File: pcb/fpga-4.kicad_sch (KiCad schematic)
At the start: 15 parts, among them U7 XC7A100T-FGG484

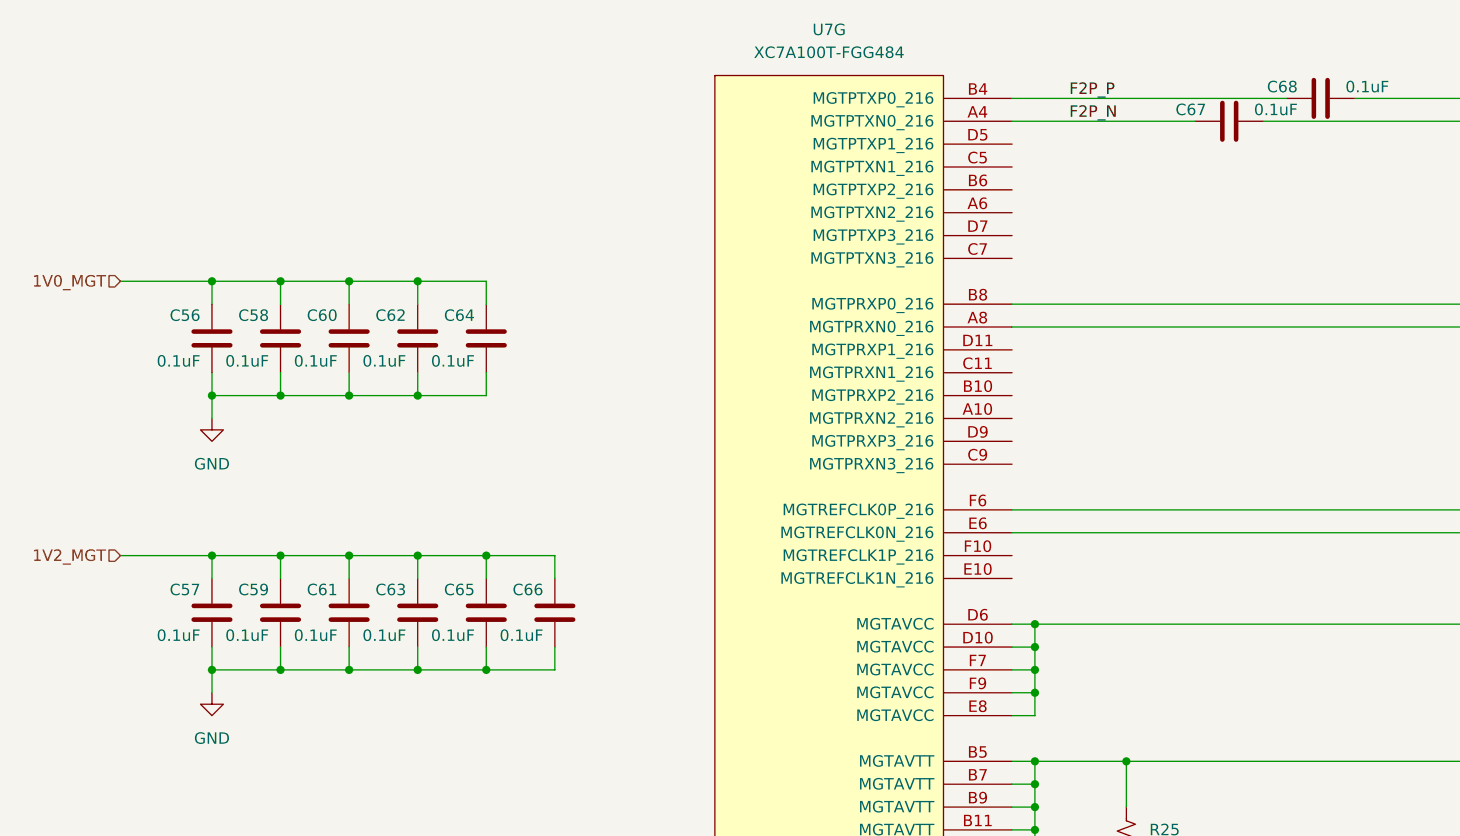
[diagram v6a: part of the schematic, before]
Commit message: added mig ddr pinout constraints
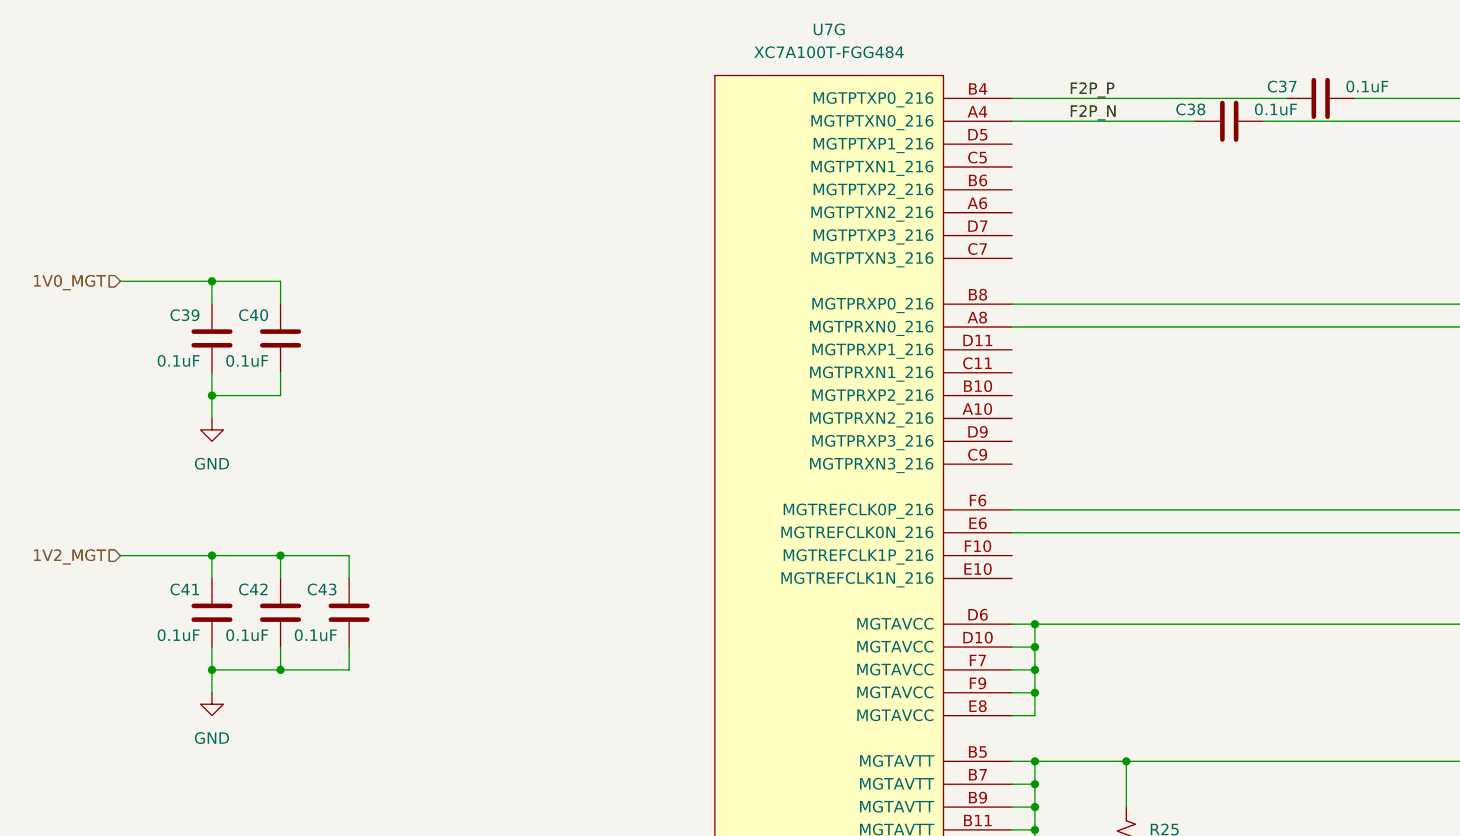
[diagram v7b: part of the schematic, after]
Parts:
- removed C60, C62, C63, C64, C65, C66: 0.1uF, Capacitor_SMD:C_0402_1005Metric, symbol library:C
- renumbered C68 to C37, C67 to C38, C56 to C39, C58 to C40, C57 to C41, C59 to C42, C61 to C43

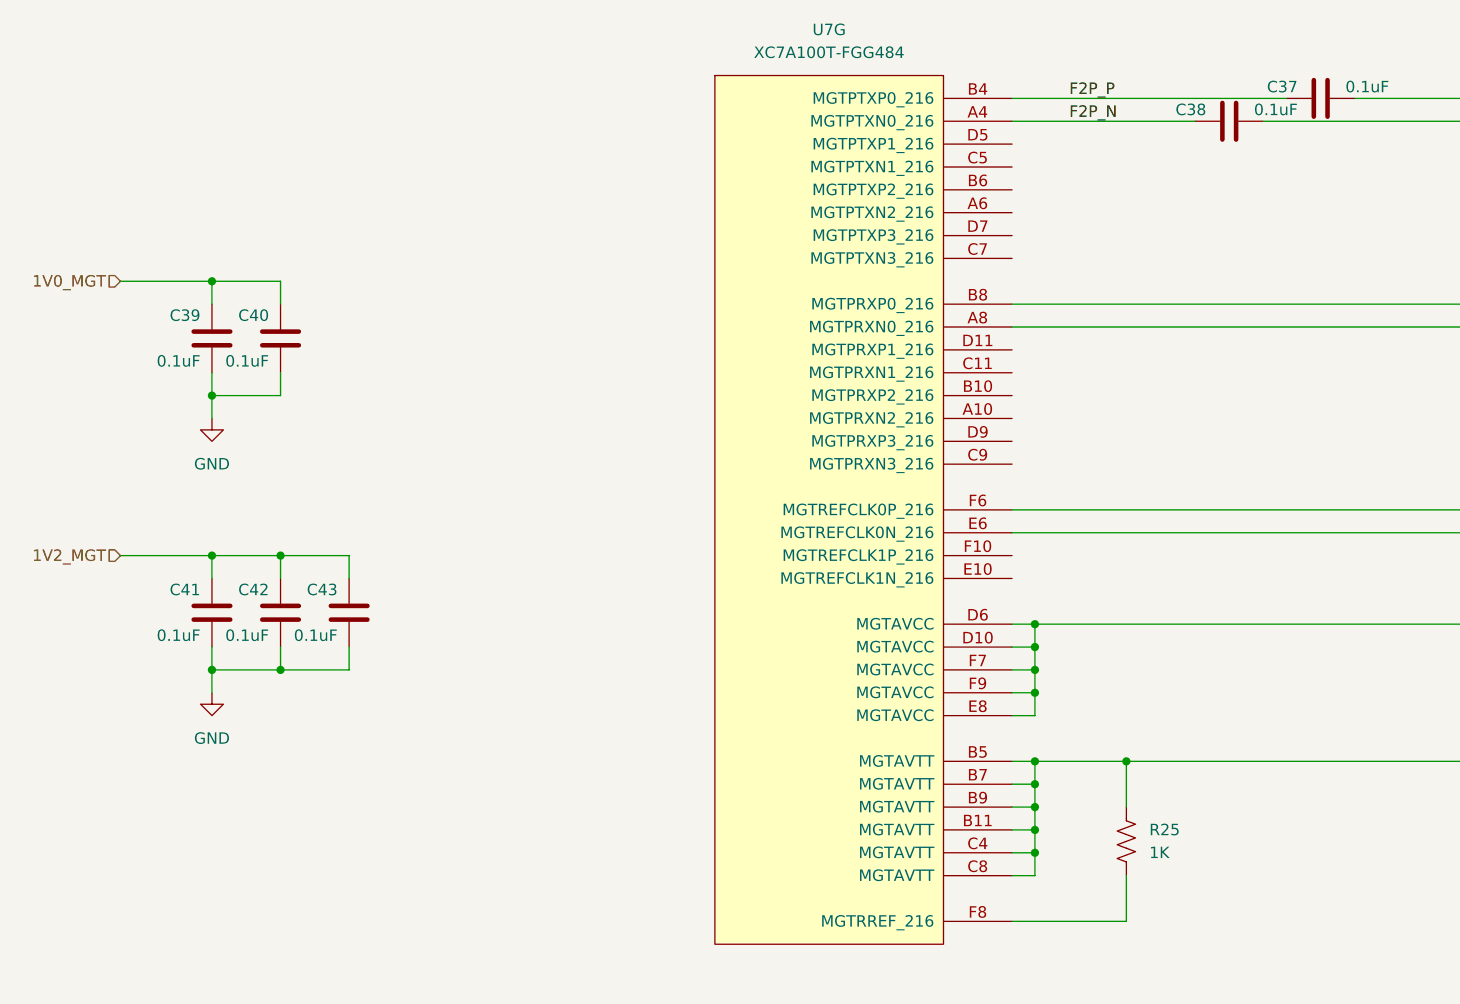
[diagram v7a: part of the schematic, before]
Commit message: restructured power, power plane layout
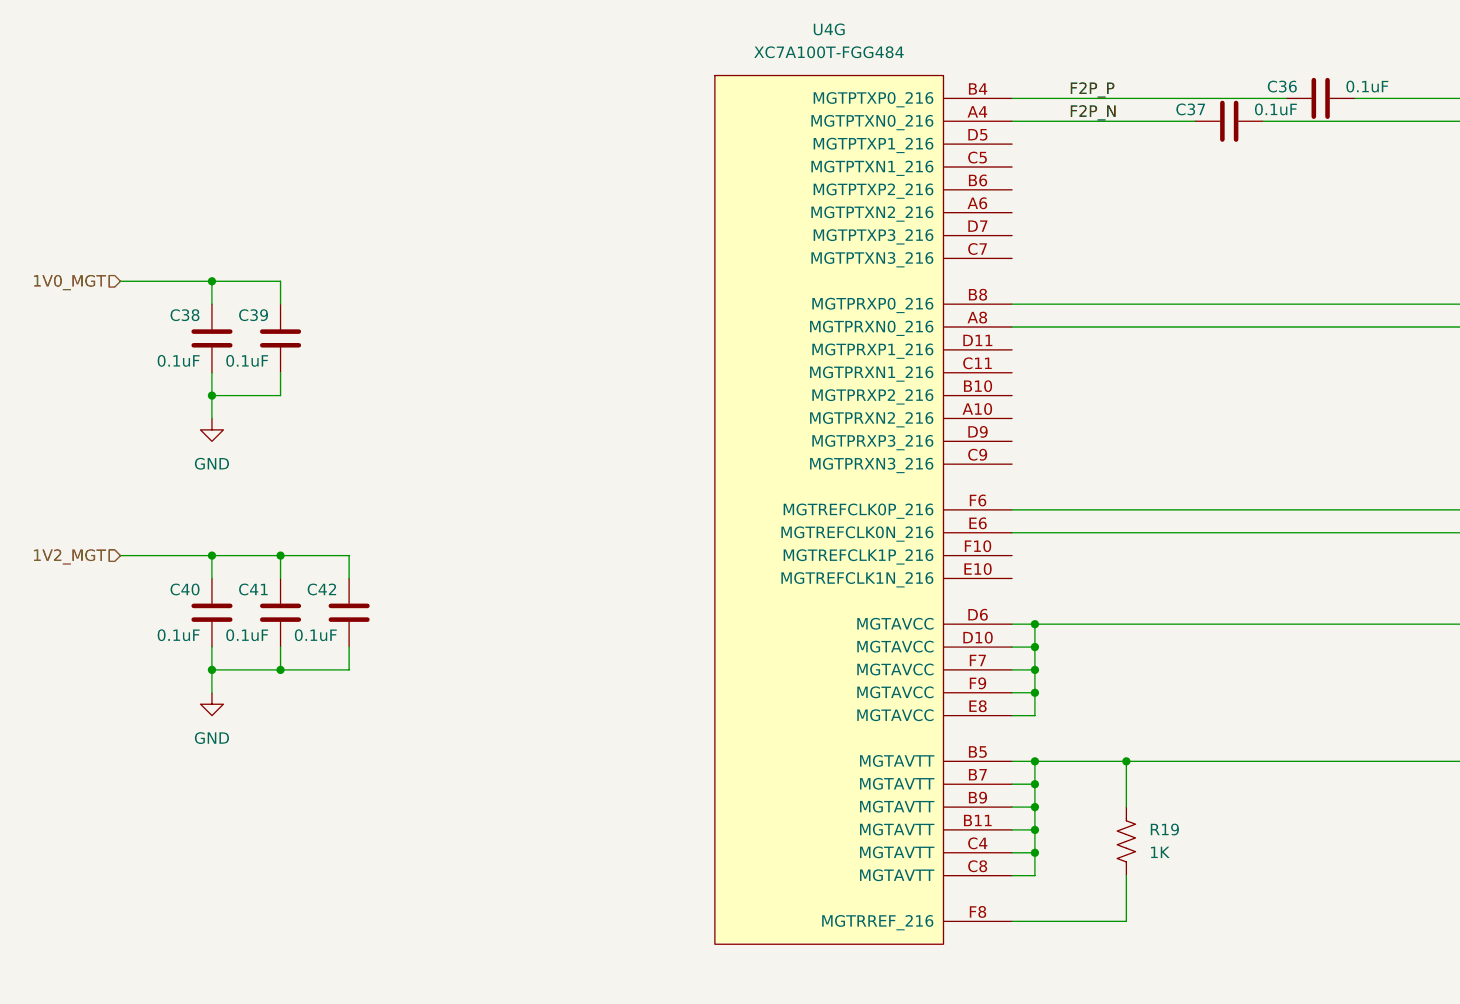
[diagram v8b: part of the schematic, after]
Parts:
- renumbered C37 to C36, C38 to C37, C39 to C38, C40 to C39, C41 to C40, C42 to C41, C43 to C42, R25 to R19, U7 to U4
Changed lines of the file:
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@@
 		(on_board yes)
 		(dnp no)
-		(property "Reference" "C39"
+		(property "Reference" "C38"
 			(at 44.45 77.47 0)
 			(effects
@@
 			(project "RPi-HwAB-1"
 				(path "/e63e39d7-6ac0-4ffd-8aa3-1841a4541b55/59d21473-a004-4514-8090-fd93db818925/1a53bf83-d036-4e40-a4d5-3697b8dd72a6"
-					(reference "C39")
+					(reference "C38")
 					(unit 1)
 				)
@@
 		(dnp no)
 		(fields_autoplaced yes)
-		(property "Reference" "U7"
+		(property "Reference" "U4"
 			(at 114.3 45.72 0)
 			(effects
@@
 			(project "RPi-HwAB-1"
 				(path "/e63e39d7-6ac0-4ffd-8aa3-1841a4541b55/59d21473-a004-4514-8090-fd93db818925/1a53bf83-d036-4e40-a4d5-3697b8dd72a6"
-					(reference "U7")
+					(reference "U4")
 					(unit 7)
 				)
@@
 		(dnp no)
 		(fields_autoplaced yes)
-		(property "Reference" "#PWR031"
+		(property "Reference" "#PWR028"
 			(at 45.72 125.73 0)
 			(effects
@@
 			(project "RPi-HwAB-1"
 				(path "/e63e39d7-6ac0-4ffd-8aa3-1841a4541b55/59d21473-a004-4514-8090-fd93db818925/1a53bf83-d036-4e40-a4d5-3697b8dd72a6"
-					(reference "#PWR031")
+					(reference "#PWR028")
 					(unit 1)
 				)
@@
 		(dnp no)
 		(fields_autoplaced yes)
-		(property "Reference" "R25"
+		(property "Reference" "R19"
 			(at 149.86 134.6199 0)
 			(effects
@@
 			(project "RPi-HwAB-1"
 				(path "/e63e39d7-6ac0-4ffd-8aa3-1841a4541b55/59d21473-a004-4514-8090-fd93db818925/1a53bf83-d036-4e40-a4d5-3697b8dd72a6"
-					(reference "R25")
+					(reference "R19")
 					(unit 1)
 				)
@@
 		(on_board yes)
 		(dnp no)
-		(property "Reference" "C37"
+		(property "Reference" "C36"
 			(at 166.37 52.07 90)
 			(effects
@@
 			(project "RPi-HwAB-1"
 				(path "/e63e39d7-6ac0-4ffd-8aa3-1841a4541b55/59d21473-a004-4514-8090-fd93db818925/1a53bf83-d036-4e40-a4d5-3697b8dd72a6"
-					(reference "C37")
+					(reference "C36")
 					(unit 1)
 				)
@@
 		(dnp no)
 		(fields_autoplaced yes)
-		(property "Reference" "#PWR030"
+		(property "Reference" "#PWR027"
 			(at 45.72 95.25 0)
 			(effects
@@
 			(project "RPi-HwAB-1"
 				(path "/e63e39d7-6ac0-4ffd-8aa3-1841a4541b55/59d21473-a004-4514-8090-fd93db818925/1a53bf83-d036-4e40-a4d5-3697b8dd72a6"
-					(reference "#PWR030")
+					(reference "#PWR027")
 					(unit 1)
 				)
@@
 		(on_board yes)
 		(dnp no)
-		(property "Reference" "C43"
+		(property "Reference" "C42"
 			(at 59.69 107.95 0)
 			(effects
@@
 			(project "RPi-HwAB-1"
 				(path "/e63e39d7-6ac0-4ffd-8aa3-1841a4541b55/59d21473-a004-4514-8090-fd93db818925/1a53bf83-d036-4e40-a4d5-3697b8dd72a6"
-					(reference "C43")
+					(reference "C42")
 					(unit 1)
 				)
@@
 		(on_board yes)
 		(dnp no)
-		(property "Reference" "C38"
+		(property "Reference" "C37"
 			(at 156.21 54.61 90)
 			(effects
@@
 			(project "RPi-HwAB-1"
 				(path "/e63e39d7-6ac0-4ffd-8aa3-1841a4541b55/59d21473-a004-4514-8090-fd93db818925/1a53bf83-d036-4e40-a4d5-3697b8dd72a6"
-					(reference "C38")
+					(reference "C37")
 					(unit 1)
 				)
@@
 		(on_board yes)
 		(dnp no)
-		(property "Reference" "C42"
+		(property "Reference" "C41"
 			(at 52.07 107.95 0)
 			(effects
@@
 			(project "RPi-HwAB-1"
 				(path "/e63e39d7-6ac0-4ffd-8aa3-1841a4541b55/59d21473-a004-4514-8090-fd93db818925/1a53bf83-d036-4e40-a4d5-3697b8dd72a6"
-					(reference "C42")
+					(reference "C41")
 					(unit 1)
 				)
@@
 		(on_board yes)
 		(dnp no)
-		(property "Reference" "C40"
+		(property "Reference" "C39"
 			(at 52.07 77.47 0)
 			(effects
@@
 			(project "RPi-HwAB-1"
 				(path "/e63e39d7-6ac0-4ffd-8aa3-1841a4541b55/59d21473-a004-4514-8090-fd93db818925/1a53bf83-d036-4e40-a4d5-3697b8dd72a6"
-					(reference "C40")
+					(reference "C39")
 					(unit 1)
 				)
@@
 		(on_board yes)
 		(dnp no)
-		(property "Reference" "C41"
+		(property "Reference" "C40"
 			(at 44.45 107.95 0)
 			(effects
@@
 			(project "RPi-HwAB-1"
 				(path "/e63e39d7-6ac0-4ffd-8aa3-1841a4541b55/59d21473-a004-4514-8090-fd93db818925/1a53bf83-d036-4e40-a4d5-3697b8dd72a6"
-					(reference "C41")
+					(reference "C40")
 					(unit 1)
 				)
